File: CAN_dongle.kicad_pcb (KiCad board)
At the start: 2 copper layers, 78 x 83 mm, 100 parts, among them J1 P0-P3, J10 K-LINE, J11 HEADER2X10, J12 SD_CARD, J13 LCD, J14 LCD_MNTHOLE, J15 LCD_MNTHOLE, J16 LCD_MNTHOLE, J17 LCD_MNTHOLE, J18 COMPR, J2 JTAG, J3 USB-MINI-A, J4 12V, J5 5V, J6 GND, J7 P4-P7, J8 CAN, J9 TERM, Q1 IRF7313, Q2 IRF7313, Q3 2N7002, Q4 2N7002, Q5 2N7002, Q6 2N7002, Q7 2N7002, SW1 SWITCH_DUALPINS, SW2 SWITCH_DUALPINS, SW3 SWITCH_DUALPINS, SW4 SWITCH_DUALPINS, U1 LM324, U2 STM32F103CBT6, U3 LM1117, U4 MC34063, U5 MCP2551, X1 XT324

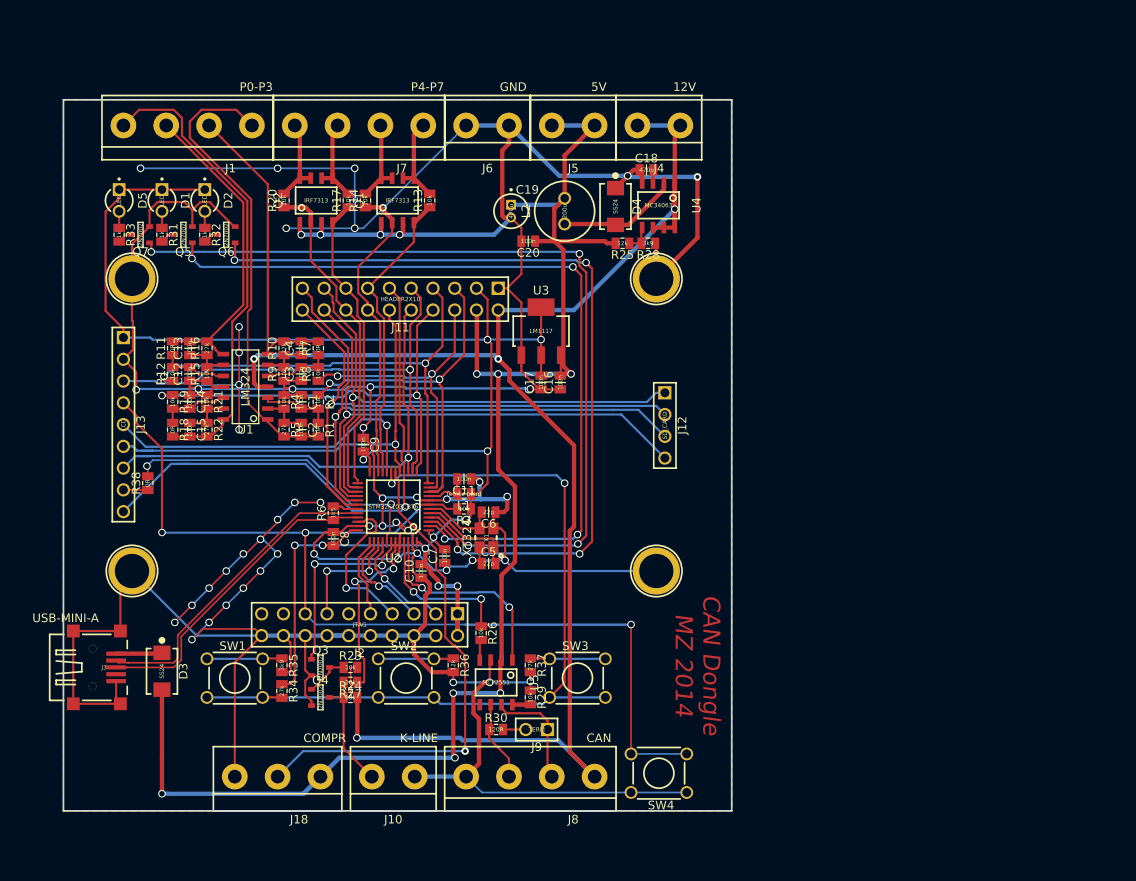
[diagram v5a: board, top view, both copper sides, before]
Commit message: Added mounting holes. Placed references ando other silkscreen texts.
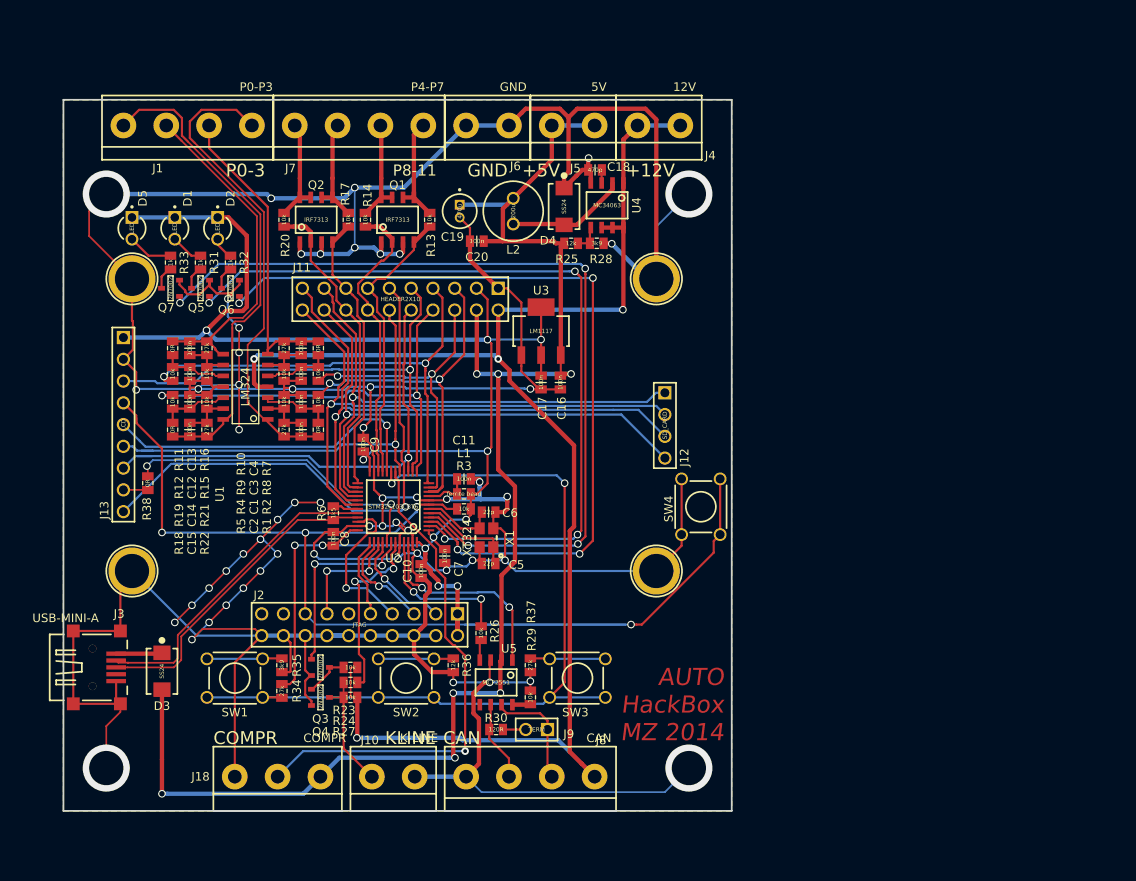
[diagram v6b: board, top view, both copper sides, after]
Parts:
- moved SW4 31.5 mm to (149.4, 97.5), turned to 90 degrees
- moved Q7 7.16 mm to (87.5, 72.0)
- moved R33 6.82 mm to (87.5, 69.0)
- moved Q5 6.56 mm to (91.0, 72.0)
- moved Q6 6.27 mm to (94.5, 72.0)
- moved C18 6.00 mm to (137.0, 58.2)
- moved C19 6.00 mm to (121.2, 63.0)
- moved C20 6.00 mm to (123.2, 66.5)
- moved D4 6.00 mm to (133.4, 62.5)
- moved L2 6.00 mm to (127.5, 63.0)
- moved R25 6.00 mm to (134.2, 66.8)
- moved R28 6.00 mm to (137.2, 66.8)
- moved U4 6.00 mm to (138.5, 62.3)
- moved R31 5.55 mm to (91.0, 69.0)
- moved R32 4.42 mm to (94.5, 69.0)
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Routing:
- net GND: track 647.2 -> 670.2 mm, vias 54 -> 57
- net +12V: track 182.7 -> 177.5 mm
- net Net-(D5-Pad2): track 1.93 -> 5.30 mm
- net Net-(Q7-Pad1): track 104.8 -> 101.5 mm
- net +5V: track 175.1 -> 172.4 mm
- net Net-(Q5-Pad1): track 97.1 -> 94.7 mm
- net Net-(J7-Pad4): track 10.3 -> 12.5 mm
- net Net-(J7-Pad3): track 10.3 -> 12.5 mm
- net Net-(J7-Pad2): track 10.0 -> 12.3 mm
- net Net-(J7-Pad1): track 10.5 -> 12.7 mm
- net /P11: track 39.4 -> 37.2 mm
- net /P10: track 35.1 -> 32.9 mm
- net Net-(C13-Pad2): track 37.3 -> 39.4 mm
- net /P9: track 36.1 -> 34.0 mm
- net Net-(Q6-Pad1): track 97.8 -> 95.9 mm
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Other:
- board text added: "+12V"
- board text added: "+5V"
- board text added: "AUTO HackBox MZ 2014"
- board text added: "CAN"
- board text added: "CANH"
- board text added: "CANL"
- board text added: "COMPR"
- board text added: "GND"
- board text added: "KLINE"
- board text added: "P0"
- board text added: "P0-3"
- board text added: "P1"
- board text added: "P10"
- board text added: "P11"
- board text added: "P2"
- board text added: "P3"
- board text added: "P8"
- board text added: "P8-11"
- board text added: "P9"
- board text removed: "CAN Dongle MZ 2014"
